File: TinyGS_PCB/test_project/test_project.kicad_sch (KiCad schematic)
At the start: 6 parts, among them J1 Power Input, U1 ESP32, U2 E32400M30S, U3 OLED

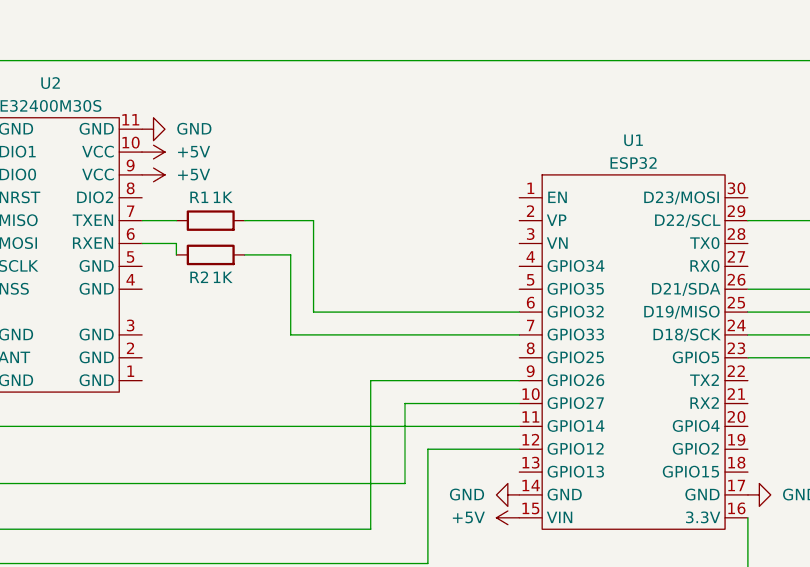
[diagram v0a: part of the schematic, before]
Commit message: fixed mistakes on pcb and software
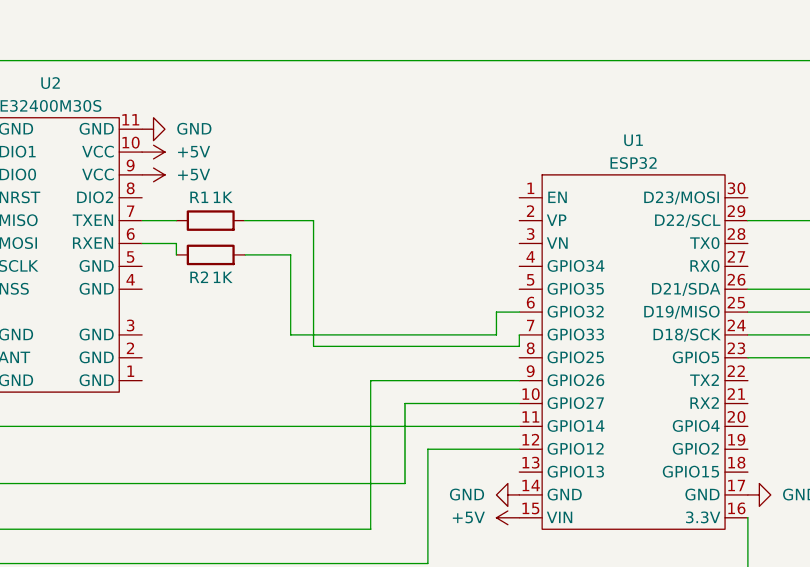
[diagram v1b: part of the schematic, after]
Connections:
- net at U1.6 (GPIO32): now also R2.2; no longer R1.2
- net at U1.7 (GPIO33): now also R1.2; no longer R2.2
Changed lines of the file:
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@@
-    (stroke (width 0) (type default) (color 0 0 0 0))
-  )
-  (wire (pts (xy 92.71 85.09) (xy 115.57 85.09))
     (stroke (width 0) (type default) (color 0 0 0 0))
   )
@@
     (stroke (width 0) (type default) (color 0 0 0 0))
   )
+  (wire (pts (xy 115.57 88.9) (xy 115.57 87.63))
+    (stroke (width 0) (type default) (color 0 0 0 0))
+  )
   (wire (pts (xy 148.59 87.63) (xy 140.97 87.63))
+    (stroke (width 0) (type default) (color 0 0 0 0))
+  )
+  (wire (pts (xy 113.03 87.63) (xy 113.03 85.09))
     (stroke (width 0) (type default) (color 0 0 0 0))
   )
@@
     (stroke (width 0) (type default) (color 0 0 0 0))
   )
+  (wire (pts (xy 113.03 85.09) (xy 115.57 85.09))
+    (stroke (width 0) (type default) (color 0 0 0 0))
+  )
   (wire (pts (xy 102.87 95.25) (xy 102.87 104.14))
     (stroke (width 0) (type default) (color 0 0 0 0))
   )
-  (wire (pts (xy 92.71 74.93) (xy 92.71 85.09))
+  (wire (pts (xy 92.71 74.93) (xy 92.71 88.9))
+    (stroke (width 0) (type default) (color 0 0 0 0))
+  )
+  (wire (pts (xy 92.71 88.9) (xy 115.57 88.9))
     (stroke (width 0) (type default) (color 0 0 0 0))
   )
@@
   )
   (wire (pts (xy 105.41 100.33) (xy 115.57 100.33))
-    (stroke (width 0) (type default) (color 0 0 0 0))
-  )
-  (wire (pts (xy 90.17 87.63) (xy 115.57 87.63))
     (stroke (width 0) (type default) (color 0 0 0 0))
   )
@@
     (stroke (width 0) (type default) (color 0 0 0 0))
   )
+  (wire (pts (xy 90.17 87.63) (xy 113.03 87.63))
+    (stroke (width 0) (type default) (color 0 0 0 0))
+  )
